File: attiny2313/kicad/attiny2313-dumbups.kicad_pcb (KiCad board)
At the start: 2 copper layers, 31.8 x 74 mm, 12 parts, among them J1 UPS_Interface, J2 AVR ISP, Q1 PN2222A, Q2 PN2222A, U2 MM232R, U3 ATtiny2313V-10P

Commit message: Add status LED to board layout
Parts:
- added D1: LED, Connector_PinHeader_2.54mm:PinHeader_1x02_P2.54mm_Vertical, F.Cu at (85.9, 104.5)
- added R7: 220, Resistor_THT:R_Axial_DIN0207_L6.3mm_D2.5mm_P10.16mm_Horizontal, F.Cu at (90.2, 107.0)
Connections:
- U3 pad 4: unconnected-(U3-Pad4) -> Net-(D1-Pad1)
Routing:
- net Net-(D1-Pad1): track 0.00 -> 7.89 mm
- net Net-(J1-Pad4): track 77.2 -> 83.3 mm
- net Net-(D1-Pad2): track 0.00 -> 4.27 mm
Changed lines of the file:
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@@
       (outputformat 1)
       (mirror false)
-      (drillshape 1)
+      (drillshape 0)
       (scaleselection 1)
-      (outputdirectory "")
+      (outputdirectory "PCB-Gerber")
     )
   )
@@
   (net 27 "unconnected-(U2-Pad16)")
   (net 28 "unconnected-(U3-Pad11)")
-  (net 29 "unconnected-(U3-Pad4)")
+  (net 29 "Net-(D1-Pad1)")
   (net 30 "unconnected-(U3-Pad6)")
   (net 31 "unconnected-(U3-Pad16)")
@@
   (net 37 "Net-(U2-Pad5)")
   (net 38 "Net-(U2-Pad7)")
+  (net 39 "Net-(D1-Pad2)")
   (footprint "Resistor_THT:R_Axial_DIN0207_L6.3mm_D2.5mm_P10.16mm_Horizontal" (layer "F.Cu")
     (at 79.61 72.08)
@@
     (fp_line (start 5.72 -5.1) (end 5.72 10.18) (layer "F.Fab") (width 0.1))
     (fp_line (start 5.72 10.18) (end -3.18 10.18) (layer "F.Fab") (width 0.1))
-    (pad "1" thru_hole roundrect locked (at 0 0) (size 1.7 1.7) (drill 1) (layers *.Cu *.Mask) (roundrect_rratio 0.147059)
+    (pad "1" thru_hole roundrect locked (at 0 0) (size 1.7 1.7) (drill 1) (layers *.Cu *.Mask) (roundrect_rratio 0.1470588235)
       (net 7 "Net-(J2-Pad1)") (pinfunction "Pin_1") (pintype "passive"))
     (pad "2" thru_hole circle locked (at 2.54 0) (size 1.7 1.7) (drill 1) (layers *.Cu *.Mask)
@@
       (net 38 "Net-(U2-Pad7)") (pinfunction "PD1") (pintype "bidirectional"))
     (pad "4" thru_hole oval locked (at 0 7.62 180) (size 1.6 1.6) (drill 0.8) (layers *.Cu *.Mask)
-      (net 29 "unconnected-(U3-Pad4)") (pinfunction "PA1/XTAL2") (pintype "bidirectional+no_connect"))
+      (net 29 "Net-(D1-Pad1)") (pinfunction "PA1/XTAL2") (pintype "bidirectional"))
     (pad "5" thru_hole oval locked (at 0 10.16 180) (size 1.6 1.6) (drill 0.8) (layers *.Cu *.Mask)
       (net 35 "Net-(Q1-Pad2)") (pinfunction "PA0/XTAL1") (pintype "bidirectional"))
@@
     )
   )
+  (footprint "Resistor_THT:R_Axial_DIN0207_L6.3mm_D2.5mm_P10.16mm_Horizontal" (layer "F.Cu")
+    (at 90.17 107 -90)
+    (descr "Resistor, Axial_DIN0207 series, Axial, Horizontal, pin pitch=10.16mm, 0.25W = 1/4W, length*diameter=6.3*2.5mm^2, http://cdn-reichelt.de/documents/datenblatt/B400/1_4W%23YAG.pdf")
+    (tags "Resistor Axial_DIN0207 series Axial Horizontal pin pitch 10.16mm 0.25W = 1/4W length 6.3mm diameter 2.5mm")
+    (property "Sheetfile" "attiny2313-dumbups.kicad_sch")
+    (property "Sheetname" "")
+    (autoplace_cost90 6)
+    (attr through_hole)
+    (fp_text reference "R7" (at 5.08 0 90) (layer "F.SilkS")
+      (effects (font (size 1 1) (thickness 0.15)))
+    )
+    (fp_text value "220" (at 5.08 2.37 90) (layer "F.Fab") hide
+      (effects (font (size 1 1) (thickness 0.15)))
+    )
+    (fp_text user "${REFERENCE}" (at 5.08 0 90) (layer "F.Fab") hide
+      (effects (font (size 1 1) (thickness 0.15)))
+    )
+    (fp_line (start 1.81 1.37) (end 8.35 1.37) (layer "F.SilkS") (width 0.12))
+    (fp_line (start 8.35 -1.37) (end 1.81 -1.37) (layer "F.SilkS") (width 0.12))
+    (fp_line (start 8.35 1.37) (end 8.35 -1.37) (layer "F.SilkS") (width 0.12))
+    (fp_line (start 9.12 0) (end 8.35 0) (layer "F.SilkS") (width 0.12))
+    (fp_line (start 1.81 -1.37) (end 1.81 1.37) (layer "F.SilkS") (width 0.12))
+    (fp_line (start 1.04 0) (end 1.81 0) (layer "F.SilkS") (width 0.12))
+    (fp_line (start -1.05 -1.5) (end -1.05 1.5) (layer "F.CrtYd") (width 0.05))
+    (fp_line (start 11.21 -1.5) (end -1.05 -1.5) (layer "F.CrtYd") (width 0.05))
+    (fp_line (start -1.05 1.5) (end 11.21 1.5) (layer "F.CrtYd") (width 0.05))
+    (fp_line (start 11.21 1.5) (end 11.21 -1.5) (layer "F.CrtYd") (width 0.05))
+    (fp_line (start 8.23 1.25) (end 8.23 -1.25) (layer "F.Fab") (width 0.1))
+    (fp_line (start 1.93 1.25) (end 8.23 1.25) (layer "F.Fab") (width 0.1))
+    (fp_line (start 0 0) (end 1.93 0) (layer "F.Fab") (width 0.1))
+    (fp_line (start 10.16 0) (end 8.23 0) (layer "F.Fab") (width 0.1))
+    (fp_line (start 8.23 -1.25) (end 1.93 -1.25) (layer "F.Fab") (width 0.1))
+    (fp_line (start 1.93 -1.25) (end 1.93 1.25) (layer "F.Fab") (width 0.1))
+    (pad "1" thru_hole circle locked (at 0 0 270) (size 1.6 1.6) (drill 0.8) (layers *.Cu *.Mask)
+      (net 39 "Net-(D1-Pad2)") (pintype "passive"))
+    (pad "2" thru_hole oval locked (at 10.16 0 270) (size 1.6 1.6) (drill 0.8) (layers *.Cu *.Mask)
+      (net 3 "Net-(J1-Pad4)") (pintype "passive"))
+    (model "${KICAD6_3DMODEL_DIR}/Resistor_THT.3dshapes/R_Axial_DIN0207_L6.3mm_D2.5mm_P10.16mm_Horizontal.wrl"
+      (offset (xyz 0 0 0))
+      (scale (xyz 1 1 1))
+      (rotate (xyz 0 0 0))
+    )
+  )
   (footprint "library:FTDI_MM232R" (layer "F.Cu")
     (at 78.78 120.34 90)
@@
       (net 27 "unconnected-(U2-Pad16)") (pinfunction "SHIELD") (pintype "input+no_connect"))
   )
+  (footprint "Connector_PinHeader_2.54mm:PinHeader_1x02_P2.54mm_Vertical" (layer "F.Cu")
+    (at 85.91 104.48)
+    (descr "Through hole straight pin header, 1x02, 2.54mm pitch, single row")
+    (tags "Through hole pin header THT 1x02 2.54mm single row")
+    (property "Sheetfile" "attiny2313-dumbups.kicad_sch")
+    (property "Sheetname" "")
+    (attr through_hole)
+    (fp_text reference "D1" (at 0 -2.33) (layer "F.SilkS")
+      (effects (font (size 1 1) (thickness 0.15)))
+    )
+    (fp_text value "LED" (at 0 4.87) (layer "F.Fab") hide
+      (effects (font (size 1 1) (thickness 0.15)))
+    )
+    (fp_text user "${REFERENCE}" (at 0 1.27 90) (layer "F.Fab") hide
+      (effects (font (size 1 1) (thickness 0.15)))
+    )
+    (fp_line (start -1.33 1.27) (end -1.33 3.87) (layer "F.SilkS") (width 0.12))
+    (fp_line (start 1.33 1.27) (end 1.33 3.87) (layer "F.SilkS") (width 0.12))
+    (fp_line (start -1.33 -1.33) (end 0 -1.33) (layer "F.SilkS") (width 0.12))
+    (fp_line (start -1.33 3.87) (end 1.33 3.87) (layer "F.SilkS") (width 0.12))
+    (fp_line (start -1.33 1.27) (end 1.33 1.27) (layer "F.SilkS") (width 0.12))
+    (fp_line (start -1.33 0) (end -1.33 -1.33) (layer "F.SilkS") (width 0.12))
+    (fp_line (start 1.8 -1.8) (end -1.8 -1.8) (layer "F.CrtYd") (width 0.05))
+    (fp_line (start 1.8 4.35) (end 1.8 -1.8) (layer "F.CrtYd") (width 0.05))
+    (fp_line (start -1.8 -1.8) (end -1.8 4.35) (layer "F.CrtYd") (width 0.05))
+    (fp_line (start -1.8 4.35) (end 1.8 4.35) (layer "F.CrtYd") (width 0.05))
+    (fp_line (start -0.635 -1.27) (end 1.27 -1.27) (layer "F.Fab") (width 0.1))
+    (fp_line (start -1.27 -0.635) (end -0.635 -1.27) (layer "F.Fab") (width 0.1))
+    (fp_line (start 1.27 3.81) (end -1.27 3.81) (layer "F.Fab") (width 0.1))
+    (fp_line (start -1.27 3.81) (end -1.27 -0.635) (layer "F.Fab") (width 0.1))
+    (fp_line (start 1.27 -1.27) (end 1.27 3.81) (layer "F.Fab") (width 0.1))
+    (pad "1" thru_hole rect locked (at 0 0) (size 1.7 1.7) (drill 1) (layers *.Cu *.Mask)
+      (net 29 "Net-(D1-Pad1)") (pinfunction "K") (pintype "passive"))
+    (pad "2" thru_hole oval locked (at 0 2.54) (size 1.7 1.7) (drill 1) (layers *.Cu *.Mask)
+      (net 39 "Net-(D1-Pad2)") (pinfunction "A") (pintype "passive"))
+    (model "${KICAD6_3DMODEL_DIR}/Connector_PinHeader_2.54mm.3dshapes/PinHeader_1x02_P2.54mm_Vertical.wrl"
+      (offset (xyz 0 0 0))
+      (scale (xyz 1 1 1))
+      (rotate (xyz 0 0 0))
+    )
+  )
   (gr_rect (start 94.07 131.16) (end 62.24 57.16) (layer "Edge.Cuts") (width 0.1) (fill none))
   (segment (start 81.04 75.18) (end 80.85 75.37) (width 0.25) (layer "B.Cu") (net 2))
@@
   (segment (start 75.5 71.6103) (end 75.5 67.520331) (width 0.25) (layer "F.Cu") (net 3))
   (segment (start 82.6147 78.725) (end 75.5 71.6103) (width 0.25) (layer "F.Cu") (net 3))
+  (segment (start 90.2 112.5) (end 89.17 111.47) (width 0.25) (layer "B.Cu") (net 3))
   (segment (start 81.6175 83.13) (end 92.98 83.13) (width 0.25) (layer "B.Cu") (net 3))
+  (segment (start 90.2 117.13) (end 90.2 112.5) (width 0.25) (layer "B.Cu") (net 3))
+  (segment (start 90.17 117.16) (end 90.2 117.13) (width 0.25) (layer "B.Cu") (net 3))
   (segment (start 90.1475 78.695) (end 92.995 78.695) (width 0.25) (layer "B.Cu") (net 3))
   (segment (start 92.995 78.695) (end 93.03 78.73) (width 0.25) (layer "B.Cu") (net 3))
@@
   (segment (start 79.61 64.725331) (end 79.655 64.680331) (width 0.25) (layer "B.Cu") (net 21))
   (segment (start 79.61 72.08) (end 79.61 64.725331) (width 0.25) (layer "B.Cu") (net 21))
+  (segment (start 85.91 104.48) (end 85.91 102.6625) (width 0.25) (layer "F.Cu") (net 29))
+  (segment (start 85.91 102.6625) (end 81.6175 98.37) (width 0.25) (layer "F.Cu") (net 29))
   (segment (start 81.6175 95.83) (end 79.73 93.9425) (width 0.25) (layer "B.Cu") (net 35))
   (segment (start 79.73 78.58) (end 80.89 77.42) (width 0.25) (layer "B.Cu") (net 35))
@@
   (segment (start 78.966489 112.553511) (end 78.966489 103.561011) (width 0.25) (layer "B.Cu") (net 38))
   (segment (start 77.51 114.01) (end 78.966489 112.553511) (width 0.25) (layer "B.Cu") (net 38))
+  (segment (start 90.17 107) (end 85.93 107) (width 0.25) (layer "B.Cu") (net 39))
+  (segment (start 85.93 107) (end 85.91 107.02) (width 0.25) (layer "B.Cu") (net 39))
 )

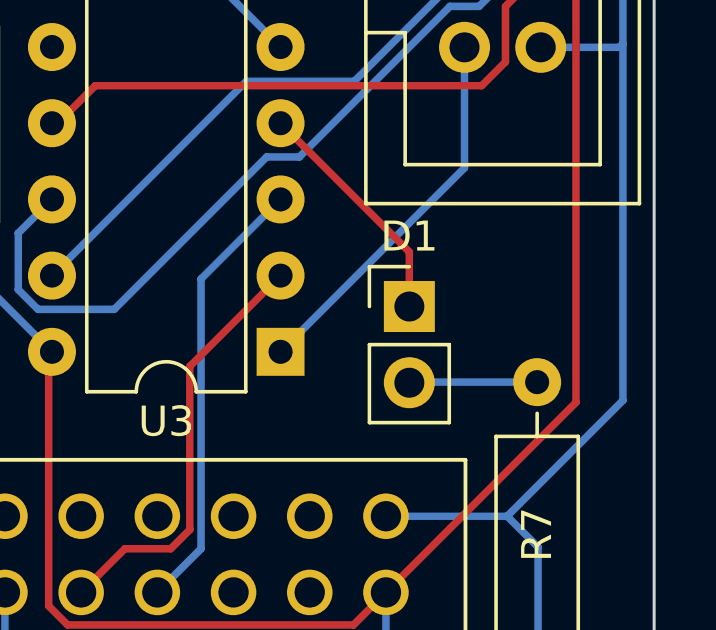
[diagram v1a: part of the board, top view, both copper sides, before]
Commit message: LED correct way around on schematic etc
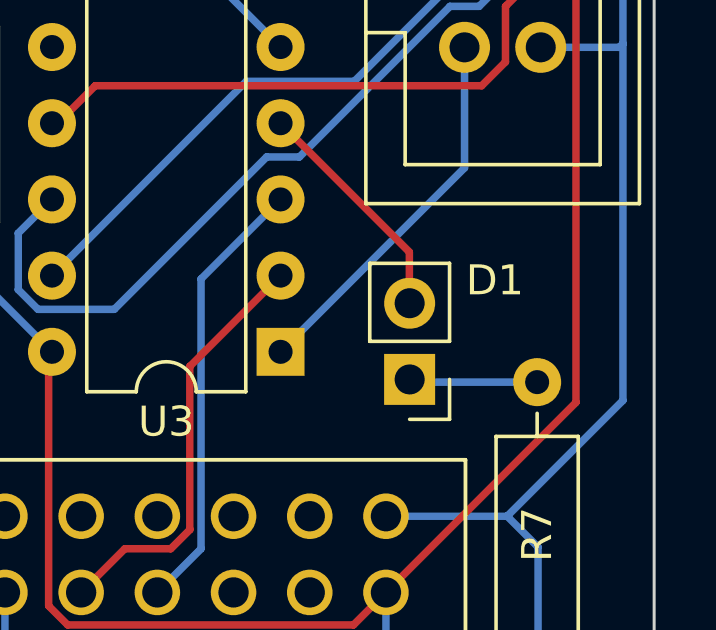
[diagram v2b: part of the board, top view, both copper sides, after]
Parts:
- moved D1 2.43 mm to (85.9, 106.9), turned to 180 degrees
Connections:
- R7 pad 1: Net-(D1-Pad2) -> Net-(D1-Pad1)
- U3 pad 4: Net-(D1-Pad1) -> Net-(D1-Pad2)
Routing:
- net Net-(D1-Pad1): track 7.89 -> 4.24 mm
- net Net-(D1-Pad2): track 4.27 -> 7.89 mm
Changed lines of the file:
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@@
       (net 38 "Net-(U2-Pad7)") (pinfunction "PD1") (pintype "bidirectional"))
     (pad "4" thru_hole oval locked (at 0 7.62 180) (size 1.6 1.6) (drill 0.8) (layers *.Cu *.Mask)
-      (net 29 "Net-(D1-Pad1)") (pinfunction "PA1/XTAL2") (pintype "bidirectional"))
+      (net 39 "Net-(D1-Pad2)") (pinfunction "PA1/XTAL2") (pintype "bidirectional"))
     (pad "5" thru_hole oval locked (at 0 10.16 180) (size 1.6 1.6) (drill 0.8) (layers *.Cu *.Mask)
       (net 35 "Net-(Q1-Pad2)") (pinfunction "PA0/XTAL1") (pintype "bidirectional"))
@@
     (fp_line (start 1.93 -1.25) (end 1.93 1.25) (layer "F.Fab") (width 0.1))
     (pad "1" thru_hole circle locked (at 0 0 270) (size 1.6 1.6) (drill 0.8) (layers *.Cu *.Mask)
-      (net 39 "Net-(D1-Pad2)") (pintype "passive"))
+      (net 29 "Net-(D1-Pad1)") (pintype "passive"))
     (pad "2" thru_hole oval locked (at 10.16 0 270) (size 1.6 1.6) (drill 0.8) (layers *.Cu *.Mask)
       (net 3 "Net-(J1-Pad4)") (pintype "passive"))
@@
   )
   (footprint "Connector_PinHeader_2.54mm:PinHeader_1x02_P2.54mm_Vertical" (layer "F.Cu")
-    (at 85.91 104.48)
+    (at 85.92 106.91 180)
     (descr "Through hole straight pin header, 1x02, 2.54mm pitch, single row")
     (tags "Through hole pin header THT 1x02 2.54mm single row")
@@
     (property "Sheetname" "")
     (attr through_hole)
-    (fp_text reference "D1" (at 0 -2.33) (layer "F.SilkS")
+    (fp_text reference "D1" (at -2.84 3.3) (layer "F.SilkS")
       (effects (font (size 1 1) (thickness 0.15)))
     )
@@
     (fp_line (start -1.27 3.81) (end -1.27 -0.635) (layer "F.Fab") (width 0.1))
     (fp_line (start 1.27 -1.27) (end 1.27 3.81) (layer "F.Fab") (width 0.1))
-    (pad "1" thru_hole rect locked (at 0 0) (size 1.7 1.7) (drill 1) (layers *.Cu *.Mask)
+    (pad "1" thru_hole rect locked (at 0 0 180) (size 1.7 1.7) (drill 1) (layers *.Cu *.Mask)
       (net 29 "Net-(D1-Pad1)") (pinfunction "K") (pintype "passive"))
-    (pad "2" thru_hole oval locked (at 0 2.54) (size 1.7 1.7) (drill 1) (layers *.Cu *.Mask)
+    (pad "2" thru_hole oval locked (at 0 2.54 180) (size 1.7 1.7) (drill 1) (layers *.Cu *.Mask)
       (net 39 "Net-(D1-Pad2)") (pinfunction "A") (pintype "passive"))
     (model "${KICAD6_3DMODEL_DIR}/Connector_PinHeader_2.54mm.3dshapes/PinHeader_1x02_P2.54mm_Vertical.wrl"
@@
   (segment (start 79.61 64.725331) (end 79.655 64.680331) (width 0.25) (layer "B.Cu") (net 21))
   (segment (start 79.61 72.08) (end 79.61 64.725331) (width 0.25) (layer "B.Cu") (net 21))
-  (segment (start 85.91 104.48) (end 85.91 102.6625) (width 0.25) (layer "F.Cu") (net 29))
-  (segment (start 85.91 102.6625) (end 81.6175 98.37) (width 0.25) (layer "F.Cu") (net 29))
+  (segment (start 90.17 107) (end 85.93 107) (width 0.25) (layer "B.Cu") (net 29))
   (segment (start 81.6175 95.83) (end 79.73 93.9425) (width 0.25) (layer "B.Cu") (net 35))
   (segment (start 79.73 78.58) (end 80.89 77.42) (width 0.25) (layer "B.Cu") (net 35))
@@
   (segment (start 78.966489 112.553511) (end 78.966489 103.561011) (width 0.25) (layer "B.Cu") (net 38))
   (segment (start 77.51 114.01) (end 78.966489 112.553511) (width 0.25) (layer "B.Cu") (net 38))
-  (segment (start 90.17 107) (end 85.93 107) (width 0.25) (layer "B.Cu") (net 39))
-  (segment (start 85.93 107) (end 85.91 107.02) (width 0.25) (layer "B.Cu") (net 39))
+  (segment (start 85.91 104.48) (end 85.91 102.6625) (width 0.25) (layer "F.Cu") (net 39))
+  (segment (start 85.91 102.6625) (end 81.6175 98.37) (width 0.25) (layer "F.Cu") (net 39))
 )
